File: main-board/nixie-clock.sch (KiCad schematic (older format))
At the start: 28 parts, among them P1 ESP8266_CONN, P2 CONN_01X06, Q1 2N7002, Q2 2N7002, SW1 ROTARY_ENCODER_SWITCH, U1 STM32F103CBT6, Y1 32.768kHz

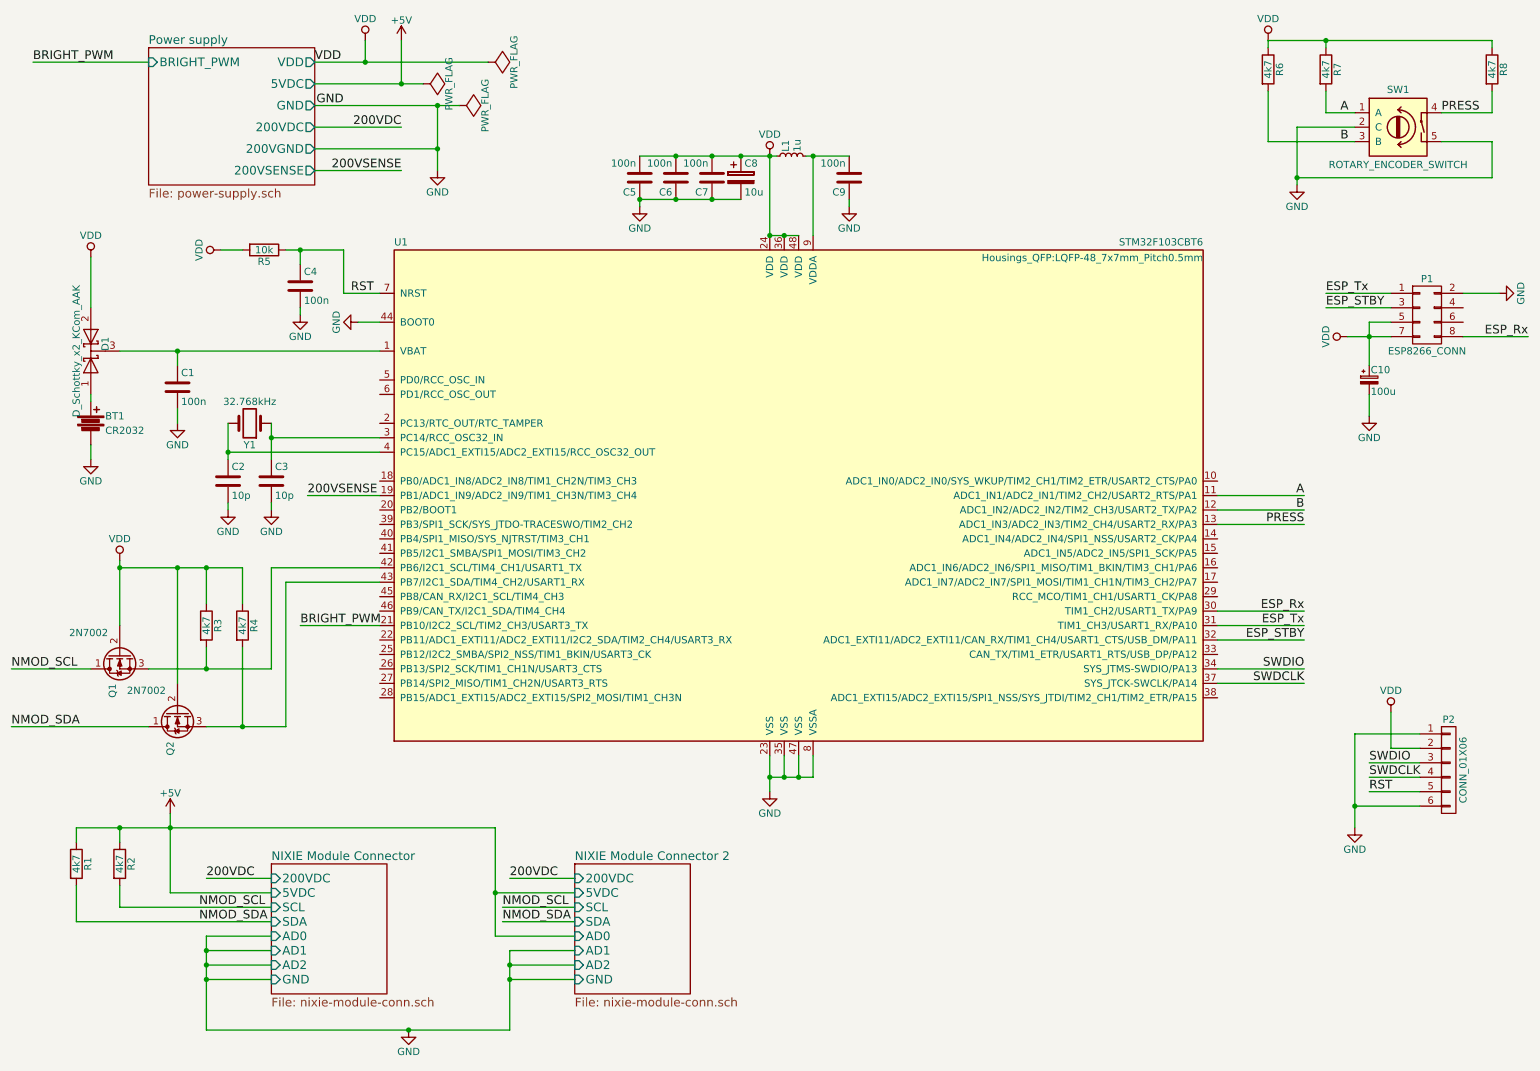
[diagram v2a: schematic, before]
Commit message: usunięcie błędnego połączenia VDD z +5V
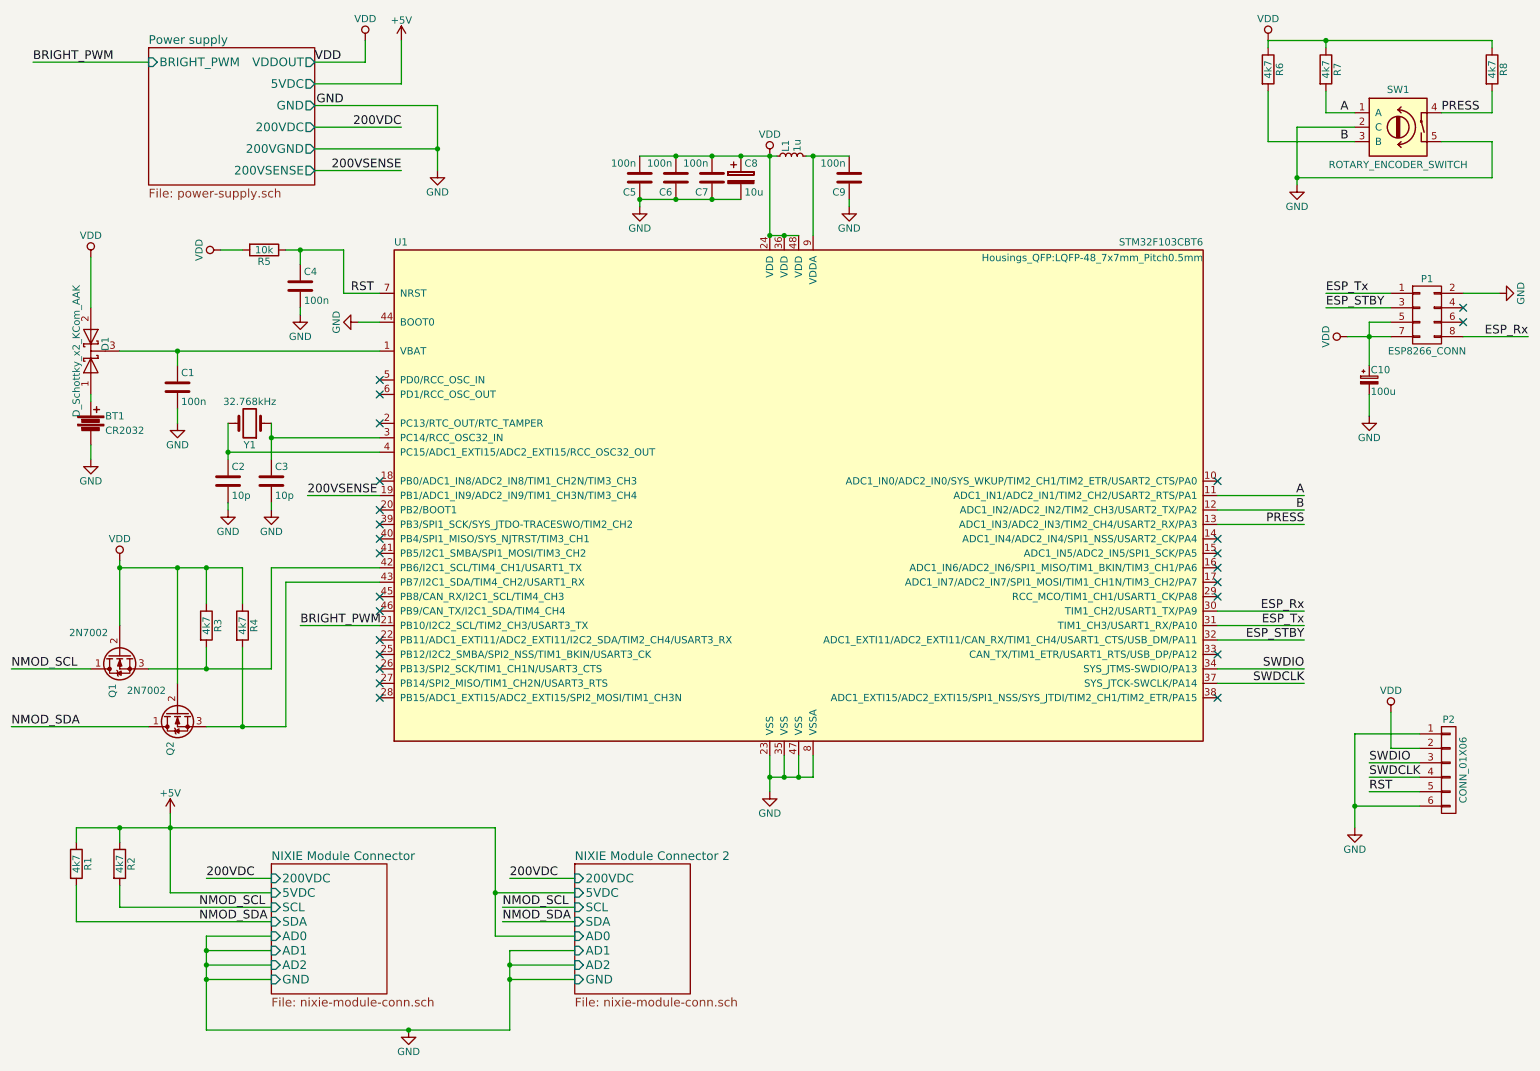
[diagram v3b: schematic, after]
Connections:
- no-connect marks 0 -> 25
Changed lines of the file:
@@
 F0 "Power supply" 60
 F1 "power-supply.sch" 60
-F2 "VDD" O R 2650 850 60
-F3 "GND" O R 2650 1150 60
-F4 "200VDC" O R 2650 1300 60
-F5 "200VGND" O R 2650 1450 60
-F6 "5VDC" O R 2650 1000 60
-F7 "BRIGHT_PWM" I L 1500 850 60
-F8 "200VSENSE" O R 2650 1600 60
+F2 "GND" O R 2650 1150 60
+F3 "200VDC" O R 2650 1300 60
+F4 "200VGND" O R 2650 1450 60
+F5 "5VDC" O R 2650 1000 60
+F6 "BRIGHT_PWM" I L 1500 850 60
+F7 "200VSENSE" O R 2650 1600 60
+F8 "VDDOUT" O R 2650 850 60
 $EndSheet
-$Comp
-L PWR_FLAG #FLG05
-U 1 1 581749DC
-P 3850 850
-F 0 "#FLG05" H 3850 945 50  0001 C CNN
-F 1 "PWR_FLAG" H 3850 1030 50  0000 C CNN
-F 2 "" H 3850 850 50  0000 C CNN
-F 3 "" H 3850 850 50  0000 C CNN
-	1    3850 850
-	0    1    1    0
-$EndComp
-$Comp
-L PWR_FLAG #FLG06
-U 1 1 58174A1B
-P 3650 1150
-F 0 "#FLG06" H 3650 1245 50  0001 C CNN
-F 1 "PWR_FLAG" H 3650 1330 50  0000 C CNN
-F 2 "" H 3650 1150 50  0000 C CNN
-F 3 "" H 3650 1150 50  0000 C CNN
-	1    3650 1150
-	0    1    1    0
-$EndComp
-Wire Wire Line
-	2650 1150 3650 1150
+Wire Wire Line
+	2650 1150 3500 1150
 Wire Wire Line
 	3500 1150 3500 1600
@@
 	1100 2200 1100 2550
 Wire Wire Line
-	2650 850  3850 850
+	3000 850  2650 850
 Text Label 2650 850  0    60   ~ 0
 VDD
@@
 Connection ~ 6000 5800
 $Comp
-L GND #PWR07
+L GND #PWR05
 U 1 1 58173306
 P 3500 1600
-F 0 "#PWR07" H 3500 1350 50  0001 C CNN
+F 0 "#PWR05" H 3500 1350 50  0001 C CNN
 F 1 "GND" H 3500 1450 50  0000 C CNN
 F 2 "" H 3500 1600 50  0000 C CNN
@@
 	1    0    0    -1
 $EndComp
-Connection ~ 3500 1150
-$Comp
-L VDD #PWR08
+$Comp
+L VDD #PWR06
 U 1 1 58175A0D
 P 3000 700
-F 0 "#PWR08" H 3000 550 50  0001 C CNN
+F 0 "#PWR06" H 3000 550 50  0001 C CNN
 F 1 "VDD" H 3000 850 50  0000 C CNN
 F 2 "" H 3000 700 50  0000 C CNN
@@
 $EndComp
 $Comp
-L VDD #PWR09
+L VDD #PWR07
 U 1 1 58176266
 P 1100 2200
-F 0 "#PWR09" H 1100 2050 50  0001 C CNN
+F 0 "#PWR07" H 1100 2050 50  0001 C CNN
 F 1 "VDD" H 1100 2350 50  0000 C CNN
 F 2 "" H 1100 2200 50  0000 C CNN
@@
 $EndComp
 $Comp
-L VDD #PWR010
+L VDD #PWR08
 U 1 1 58176451
 P 5800 1500
-F 0 "#PWR010" H 5800 1350 50  0001 C CNN
+F 0 "#PWR08" H 5800 1350 50  0001 C CNN
 F 1 "VDD" H 5800 1650 50  0000 C CNN
 F 2 "" H 5800 1500 50  0000 C CNN
@@
 	1    0    0    -1
 $EndComp
-Connection ~ 3000 850
 $Comp
 L CONN_02X04 P1
@@
 	10600 2450 10850 2450
 $Comp
-L GND #PWR011
+L GND #PWR09
 U 1 1 5817B257
 P 10850 2450
-F 0 "#PWR011" H 10850 2200 50  0001 C CNN
+F 0 "#PWR09" H 10850 2200 50  0001 C CNN
 F 1 "GND" H 10850 2300 50  0000 C CNN
 F 2 "" H 10850 2450 50  0000 C CNN
@@
 $EndComp
 $Comp
-L VDD #PWR012
+L VDD #PWR010
 U 1 1 5817B5C8
 P 9800 2750
-F 0 "#PWR012" H 9800 2600 50  0001 C CNN
+F 0 "#PWR010" H 9800 2600 50  0001 C CNN
 F 1 "VDD" H 9800 2900 50  0000 C CNN
 F 2 "" H 9800 2750 50  0000 C CNN
@@
 	2650 1300 3250 1300
 Wire Wire Line
-	2650 1000 3400 1000
+	2650 1000 3250 1000
 Text Label 3250 1300 2    60   ~ 0
 200VDC
@@
 	3900 6600 4450 6600
 $Comp
-L GND #PWR013
+L GND #PWR011
 U 1 1 5819F48F
 P 3300 7550
-F 0 "#PWR013" H 3300 7300 50  0001 C CNN
+F 0 "#PWR011" H 3300 7300 50  0001 C CNN
 F 1 "GND" H 3300 7400 50  0000 C CNN
 F 2 "" H 3300 7550 50  0000 C CNN
@@
 NMOD_SDA
 $Comp
-L PWR_FLAG #FLG014
-U 1 1 58212F70
-P 3400 1000
-F 0 "#FLG014" H 3400 1095 50  0001 C CNN
-F 1 "PWR_FLAG" H 3400 1180 50  0000 C CNN
-F 2 "" H 3400 1000 50  0000 C CNN
-F 3 "" H 3400 1000 50  0000 C CNN
-	1    3400 1000
-	0    1    1    0
-$EndComp
-$Comp
-L +5V #PWR015
+L +5V #PWR012
 U 1 1 58214622
 P 3250 700
-F 0 "#PWR015" H 3250 550 50  0001 C CNN
+F 0 "#PWR012" H 3250 550 50  0001 C CNN
 F 1 "+5V" H 3250 840 50  0000 C CNN
 F 2 "" H 3250 700 50  0000 C CNN
@@
 $EndComp
 Wire Wire Line
-	3250 700  3250 1000
-Connection ~ 3250 1000
-$Comp
-L +5V #PWR016
+	3250 1000 3250 700
+$Comp
+L +5V #PWR013
 U 1 1 5821ADB1
 P 1650 6050
-F 0 "#PWR016" H 1650 5900 50  0001 C CNN
+F 0 "#PWR013" H 1650 5900 50  0001 C CNN
 F 1 "+5V" H 1650 6190 50  0000 C CNN
 F 2 "" H 1650 6050 50  0000 C CNN
@@
 Connection ~ 1300 6150
 $Comp
-L GND #PWR017
+L GND #PWR014
 U 1 1 5822B6A3
 P 9950 3300
-F 0 "#PWR017" H 9950 3050 50  0001 C CNN
+F 0 "#PWR014" H 9950 3050 50  0001 C CNN
 F 1 "GND" H 9950 3150 50  0000 C CNN
 F 2 "" H 9950 3300 50  0000 C CNN
@@
 $EndComp
 $Comp
-L GND #PWR018
+L GND #PWR015
 U 1 1 5823EC3A
 P 4900 1850
-F 0 "#PWR018" H 4900 1600 50  0001 C CNN
+F 0 "#PWR015" H 4900 1600 50  0001 C CNN
 F 1 "GND" H 4900 1700 50  0000 C CNN
 F 2 "" H 4900 1850 50  0000 C CNN
@@
 $EndComp
 $Comp
-L GND #PWR019
+L GND #PWR016
 U 1 1 58241A1B
 P 6350 1850
-F 0 "#PWR019" H 6350 1600 50  0001 C CNN
+F 0 "#PWR016" H 6350 1600 50  0001 C CNN
 F 1 "GND" H 6350 1700 50  0000 C CNN
 F 2 "" H 6350 1850 50  0000 C CNN
@@
 Connection ~ 5600 1500
 $Comp
-L GND #PWR020
+L GND #PWR017
 U 1 1 5822205E
 P 5800 5900
-F 0 "#PWR020" H 5800 5650 50  0001 C CNN
+F 0 "#PWR017" H 5800 5650 50  0001 C CNN
 F 1 "GND" H 5800 5750 50  0000 C CNN
 F 2 "" H 5800 5900 50  0000 C CNN
@@
 $EndComp
 $Comp
-L GND #PWR021
+L GND #PWR018
 U 1 1 58281FC0
 P 9450 1700
-F 0 "#PWR021" H 9450 1450 50  0001 C CNN
+F 0 "#PWR018" H 9450 1450 50  0001 C CNN
 F 1 "GND" H 9450 1550 50  0000 C CNN
 F 2 "" H 9450 1700 50  0000 C CNN
@@
 $EndComp
 $Comp
-L GND #PWR022
+L GND #PWR019
 U 1 1 5829D7A9
 P 9850 6150
-F 0 "#PWR022" H 9850 5900 50  0001 C CNN
+F 0 "#PWR019" H 9850 5900 50  0001 C CNN
 F 1 "GND" H 9850 6000 50  0000 C CNN
 F 2 "" H 9850 6150 50  0000 C CNN
@@
 Connection ~ 9850 6000
 $Comp
-L VDD #PWR023
+L VDD #PWR020
 U 1 1 582A0114
 P 9250 700
-F 0 "#PWR023" H 9250 550 50  0001 C CNN
+F 0 "#PWR020" H 9250 550 50  0001 C CNN
 F 1 "VDD" H 9250 850 50  0000 C CNN
 F 2 "" H 9250 700 50  0000 C CNN
@@
 $EndComp
 $Comp
-L VDD #PWR024
+L VDD #PWR021
 U 1 1 582A0479
 P 10100 5350
-F 0 "#PWR024" H 10100 5200 50  0001 C CNN
+F 0 "#PWR021" H 10100 5200 50  0001 C CNN
 F 1 "VDD" H 10100 5500 50  0000 C CNN
 F 2 "" H 10100 5350 50  0000 C CNN
@@
 $EndComp
 $Comp
-L GND #PWR025
+L GND #PWR022
 U 1 1 582A7C03
 P 2550 2600
-F 0 "#PWR025" H 2550 2350 50  0001 C CNN
+F 0 "#PWR022" H 2550 2350 50  0001 C CNN
 F 1 "GND" H 2550 2450 50  0000 C CNN
 F 2 "" H 2550 2600 50  0000 C CNN
@@
 $EndComp
 $Comp
-L VDD #PWR026
+L VDD #PWR023
 U 1 1 582A7F9C
 P 2000 2150
-F 0 "#PWR026" H 2000 2000 50  0001 C CNN
+F 0 "#PWR023" H 2000 2000 50  0001 C CNN
 F 1 "VDD" H 2000 2300 50  0000 C CNN
 F 2 "" H 2000 2150 50  0000 C CNN
@@
 RST
 $Comp
-L GND #PWR027
+L GND #PWR024
 U 1 1 582ABAFC
 P 2950 2650
-F 0 "#PWR027" H 2950 2400 50  0001 C CNN
+F 0 "#PWR024" H 2950 2400 50  0001 C CNN
 F 1 "GND" H 2950 2500 50  0000 C CNN
 F 2 "" H 2950 2650 50  0000 C CNN
@@
 	2550 4750 3100 4750
 $Comp
-L VDD #PWR028
+L VDD #PWR025
 U 1 1 58311767
 P 1300 4300
-F 0 "#PWR028" H 1300 4150 50  0001 C CNN
+F 0 "#PWR025" H 1300 4150 50  0001 C CNN
 F 1 "VDD" H 1300 4450 50  0000 C CNN
 F 2 "" H 1300 4300 50  0000 C CNN
@@
 	2450 5450 2450 4450
 Connection ~ 2150 5450
+NoConn ~ 10600 2550
+NoConn ~ 10600 2650
+NoConn ~ 8900 3750
+NoConn ~ 8900 4150
+NoConn ~ 8900 4250
+NoConn ~ 8900 4350
+NoConn ~ 8900 4450
+NoConn ~ 8900 4550
+NoConn ~ 8900 4950
+NoConn ~ 8900 5250
+NoConn ~ 3100 5250
+NoConn ~ 3100 5150
+NoConn ~ 3100 5050
+NoConn ~ 3100 4950
+NoConn ~ 3100 4850
+NoConn ~ 3100 4650
+NoConn ~ 3100 4550
+NoConn ~ 3100 4250
+NoConn ~ 3100 4150
+NoConn ~ 3100 4050
+NoConn ~ 3100 3950
+NoConn ~ 3100 3750
+NoConn ~ 3100 3350
+NoConn ~ 3100 3150
+NoConn ~ 3100 3050
 $EndSCHEMATC

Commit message: poprawki prowadzenia ścieżek, footprintów, zmniejszenie rozmiaru płytki pod lampę nixie
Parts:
- BT1: symbol Battery -> Battery-RESCUE-nixie-clock
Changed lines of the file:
@@
 EESchema Schematic File Version 2
+LIBS:nixie-clock-rescue
 LIBS:power
 LIBS:device
@@
 LIBS:contrib
 LIBS:valves
-LIBS:stm32
-LIBS:sensors
 LIBS:nixie-clock-cache
-EELAYER 25 0
+EELAYER 26 0
 EELAYER END
 $Descr A4 11693 8268
@@
 	1700 3350 1700 3250
 $Comp
-L Battery BT1
+L Battery-RESCUE-nixie-clock BT1
 U 1 1 580A0D26
 P 1100 3350
